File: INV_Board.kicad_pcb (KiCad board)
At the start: 4 copper layers, 84 x 66.5 mm, 192 parts, among them J1 USB_B_Micro, J10 Conn_01x02_Male, J11 Conn_01x04_Male, J12 Conn_01x06_Female, J2 Conn_01x02_Male, J3 Conn_01x02_Male, J4 Conn_01x02_Male, J6 Conn_01x08_Female, J7 Conn_01x03_Male, J8 Conn_ARM_JTAG_SWD_10, J9 Conn_01x06_Male, Q1 Q_NMOS_GDS, Q10 IPT015N10N5, Q11 IPT015N10N5, Q12 IPT015N10N5, Q2 Q_NMOS_GDS, Q3 Q_NMOS_GDS, Q4 Q_NMOS_GDS, Q5 Q_NMOS_GDS, Q6 Q_NMOS_GDS, Q7 IPT015N10N5, Q8 IPT015N10N5, Q9 IPT015N10N5, U1 INA181, U10 INA181, U2 STM32F303CBTx, U3 IR2181, U4 IR2181, U5 IR2181, U6 TPS76333, U7 LM5017MR, U8 TPS61041DDC, U9 INA181, X1 ASE-xxxMHz

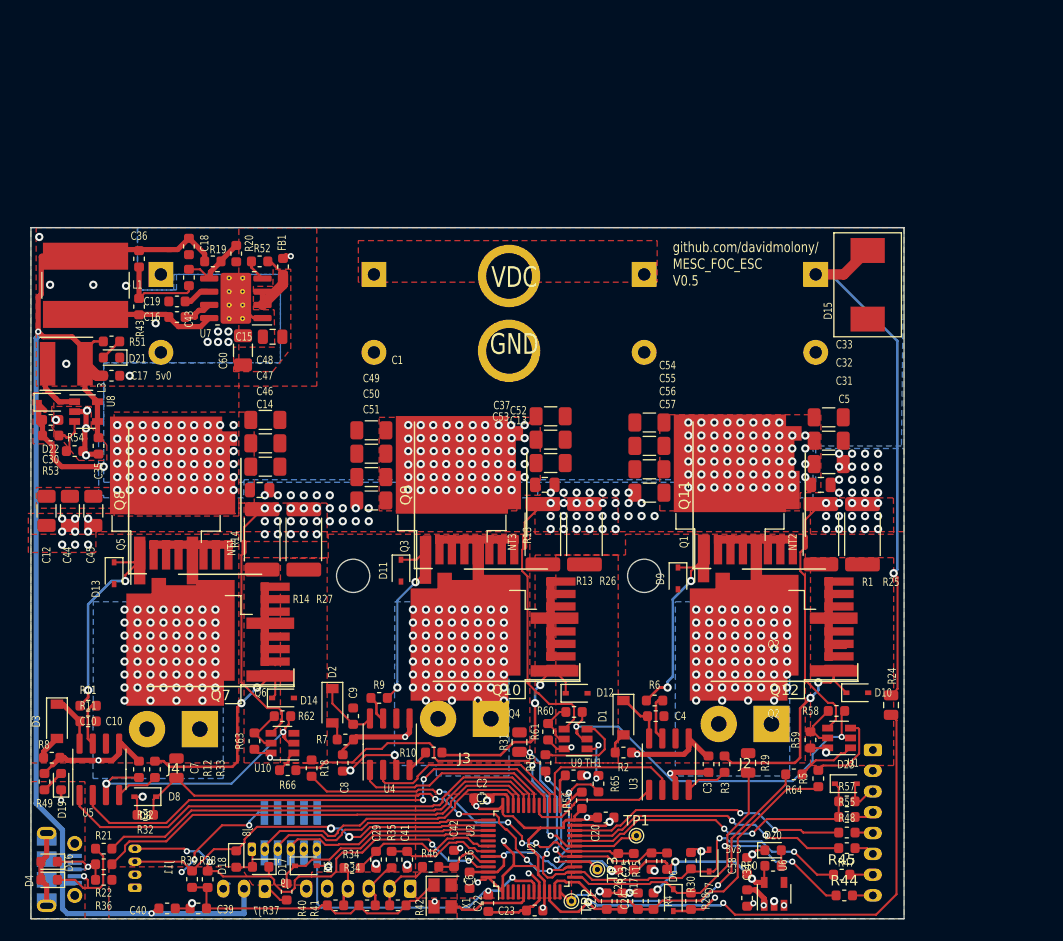
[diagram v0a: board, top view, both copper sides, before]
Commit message: WIP Rearrange power stage to further reduce inductance and reduce board size by 10mm
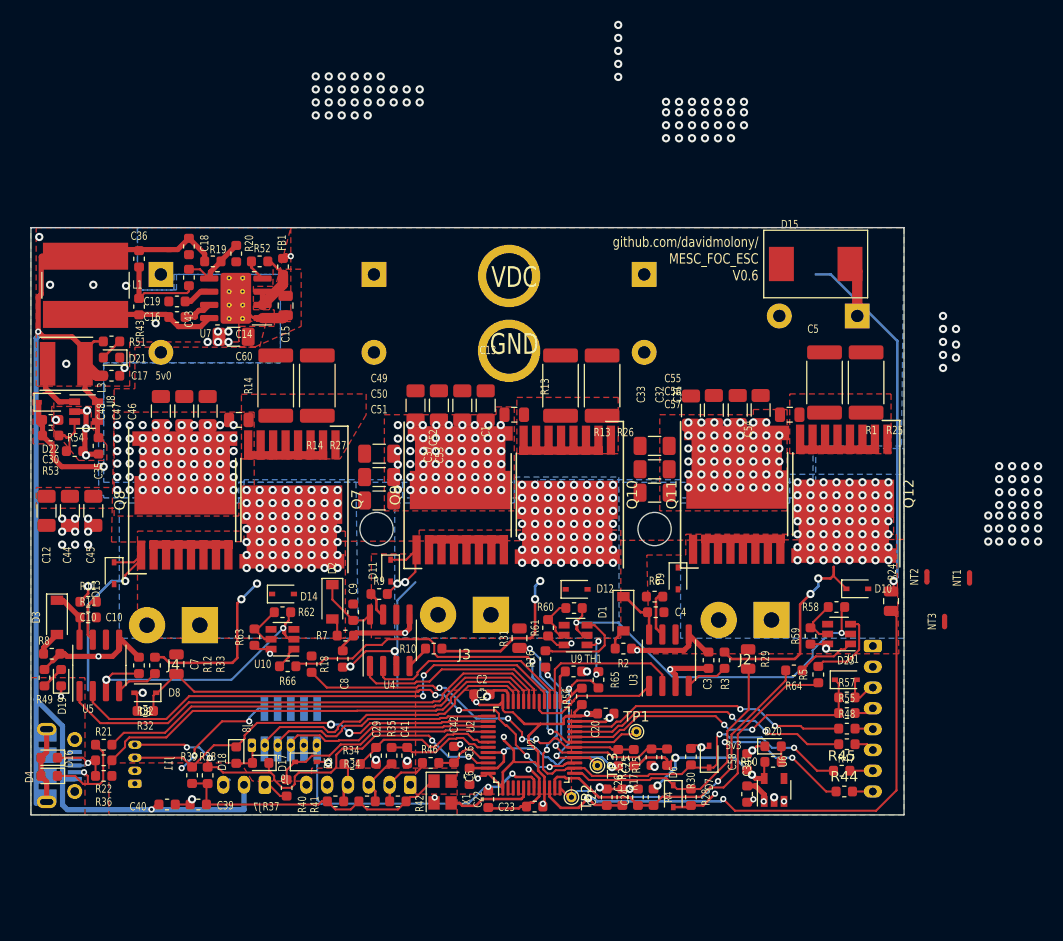
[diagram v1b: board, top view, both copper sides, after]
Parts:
- removed Q1, Q2, Q3, Q4, Q5, Q6: Q_NMOS_GDS, Package_TO_SOT_SMD:TO-263-2
- moved NT1 69.9 mm to (206.3, 82.7)
- moved NT3 41.1 mm to (203.9, 86.9)
- moved R14 14.9 mm to (139.6, 64.2)
- moved R27 14.9 mm to (143.6, 64.2)
- moved R1 14.6 mm to (192.3, 63.9)
- moved R25 14.6 mm to (196.3, 63.9)
- moved R13 14.4 mm to (166.9, 64.2)
- moved R26 14.4 mm to (170.9, 64.2)
- moved Q7 14.3 mm to (141.1, 75.2), turned to 270 degrees
- moved Q12 13.9 mm to (194.2, 74.6), turned to 270 degrees
- moved Q10 13.8 mm to (167.6, 74.7), turned to 270 degrees
- moved NT2 12.2 mm to (202.2, 82.6)
- moved C33 11.1 mm to (181.7, 66.5), turned to 90 degrees
- moved C37 10.8 mm to (155.2, 66.1), turned to 90 degrees
- moved C48 10.1 mm to (128.5, 66.7), turned to 90 degrees
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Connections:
- C13 pad 2: GND -> ISV
- C14 pad 2: GND -> ISW
- C5 pad 2: GND -> ISU
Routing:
- net +12V: track 129.7 -> 94.8 mm
- net SGV: track 21.4 -> 0.00 mm
- net SGW: track 20.2 -> 0.00 mm
- net SGU: track 19.8 -> 0.15 mm
- net /UGH: track 19.4 -> 0.00 mm, vias 2 -> 0
- net +VDC: track 53.1 -> 40.9 mm, vias 178 -> 175
- net GND: track 170.7 -> 161.5 mm, vias 144 -> 94
- net /VGL: track 20.1 -> 15.2 mm
- net SWU: track 0.00 -> 4.44 mm, vias 60 -> 56
- net /WGL: track 20.4 -> 16.4 mm
- net ISU: track 9.53 -> 7.83 mm, vias 0 -> 1
- net ISW: track 0.78 -> 0.00 mm
- net SWW: vias 60 -> 79
- net SWV: vias 60 -> 80
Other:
- board size 84 x 66.5 mm -> 84 x 56.5 mm
- board text added: "github.com/davidmolony/ MESC_FOC_ESC V0.6"
- board text removed: "github.com/davidmolony/ MESC_FOC_ESC V0.5"

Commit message: Incomplete smaller, lower inductance option. might not be good since thermal capacit will be reduced.
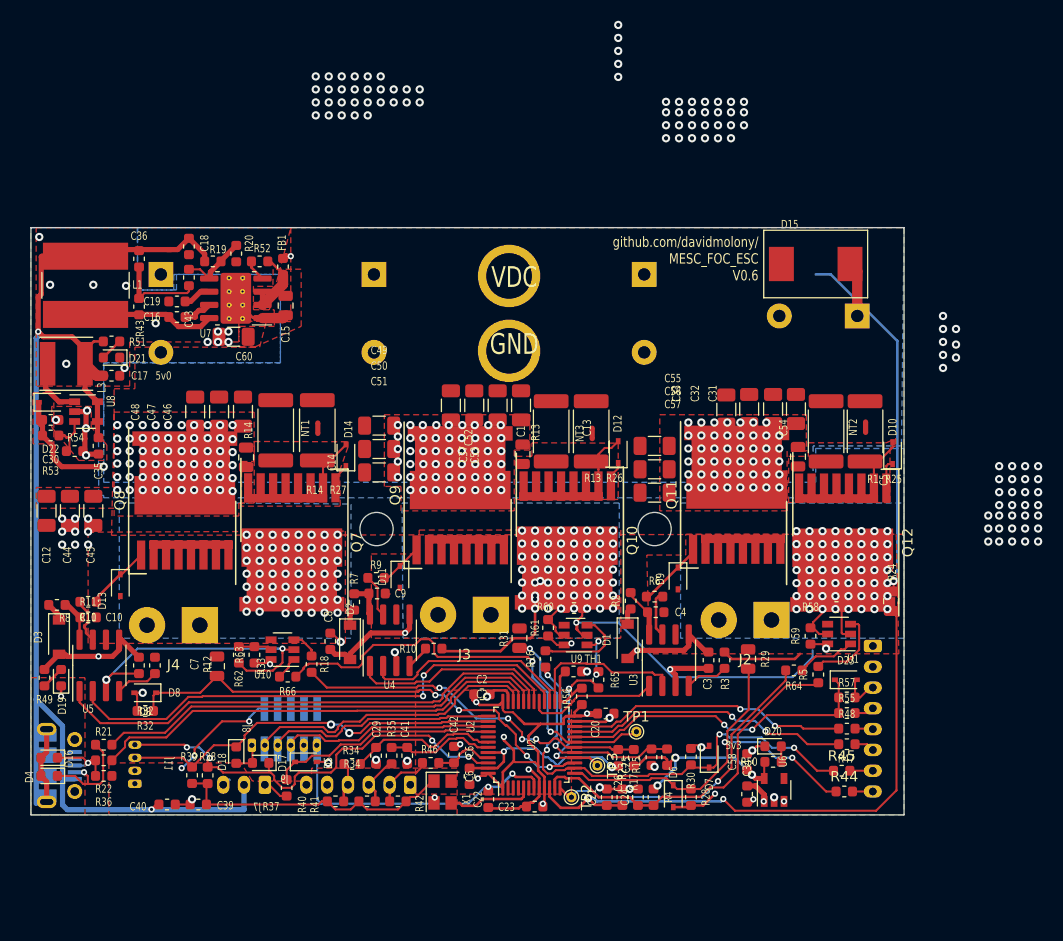
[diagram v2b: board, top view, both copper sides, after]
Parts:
- moved NT1 64.3 mm to (143.6, 68.3)
- moved NT3 38.4 mm to (170.0, 68.8)
- moved NT2 15.6 mm to (196.3, 68.2)
- moved D14 14.7 mm to (146.3, 70.9), turned to 90 degrees
- moved D12 13.8 mm to (172.5, 70.6), turned to 90 degrees
- moved D10 13.5 mm to (198.9, 70.7), turned to 90 degrees
- moved R62 5.87 mm to (136.0, 90.1), turned to 270 degrees
- moved R8 4.73 mm to (118.5, 85.3), turned to 0 degrees
- moved R1 4.70 mm to (192.5, 68.6)
- moved Q12 4.70 mm to (194.1, 79.3)
- moved R25 4.70 mm to (196.2, 68.6)
- moved R2 4.65 mm to (173.7, 84.9), turned to 90 degrees
- moved R26 4.52 mm to (169.9, 68.6)
- moved R13 4.49 mm to (166.1, 68.6)
- moved Q10 4.40 mm to (167.6, 79.1)
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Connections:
- D1 pad 1: Net-(C4-Pad1) -> Net-(D1-Pad1)
- D1 pad 2: Net-(D1-Pad2) -> +12V
- D2 pad 1: Net-(C9-Pad1) -> Net-(D2-Pad1)
- D2 pad 2: Net-(D2-Pad2) -> +12V
- D3 pad 1: Net-(C10-Pad1) -> Net-(D3-Pad1)
- D3 pad 2: Net-(D3-Pad2) -> +12V
- R2 pad 1: +12V -> Net-(D1-Pad1)
- R2 pad 2: Net-(D1-Pad2) -> Net-(C4-Pad1)
- R7 pad 1: +12V -> Net-(D2-Pad1)
- R7 pad 2: Net-(D2-Pad2) -> Net-(C9-Pad1)
- R8 pad 1: +12V -> Net-(D3-Pad1)
- R8 pad 2: Net-(D3-Pad2) -> Net-(C10-Pad1)
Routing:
- net /WGL: track 16.4 -> 2.49 mm, vias 2 -> 0
- net /VGH: track 17.8 -> 4.18 mm, vias 2 -> 0
- net /WGH: track 21.5 -> 7.85 mm, vias 2 -> 0
- net /UGL: track 20.8 -> 10.6 mm, vias 2 -> 0
- net ISW: track 0.00 -> 7.79 mm
- net /UGH: track 0.00 -> 6.55 mm
- net GND: track 161.5 -> 155.9 mm, vias 94 -> 93
- net ISV: track 9.05 -> 14.5 mm
- net ISU: track 7.83 -> 13.0 mm
- net Net-(C9-Pad1): track 6.11 -> 3.49 mm
- net /VGL: track 15.2 -> 17.7 mm
- net Net-(D3-Pad2): track 2.38 -> 0.00 mm
- net +12V: track 94.8 -> 96.9 mm
- net Net-(D1-Pad2): track 2.03 -> 0.00 mm
- net Net-(D3-Pad1): track 0.00 -> 1.86 mm
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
